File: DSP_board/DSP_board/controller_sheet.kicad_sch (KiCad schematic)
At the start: 29 parts, among them IC5 F280025CPNQR, J1 Conn_01x02, J2 Conn_01x02, J3 Conn_01x02, J4 Conn_01x02, J5 1-84981-0, J6 Conn_01x02

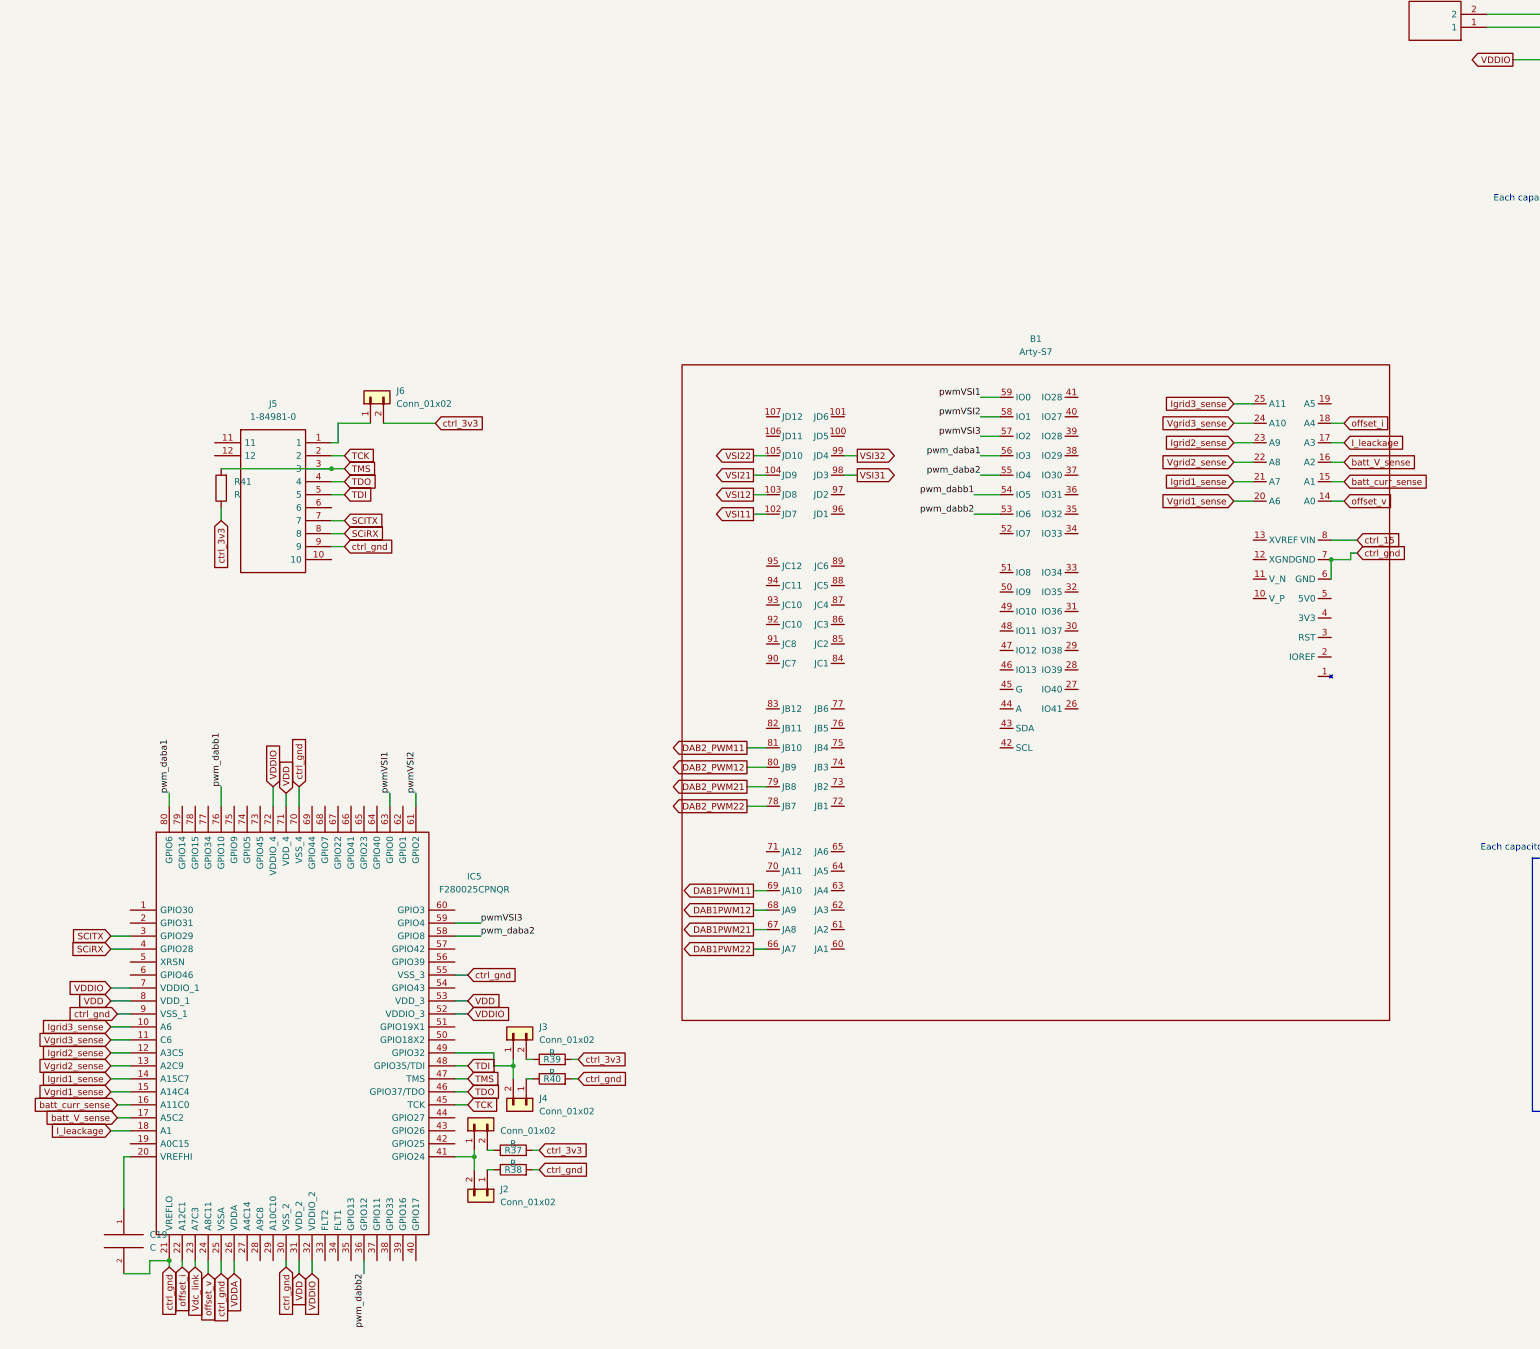
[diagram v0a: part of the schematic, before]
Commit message: adding diodes
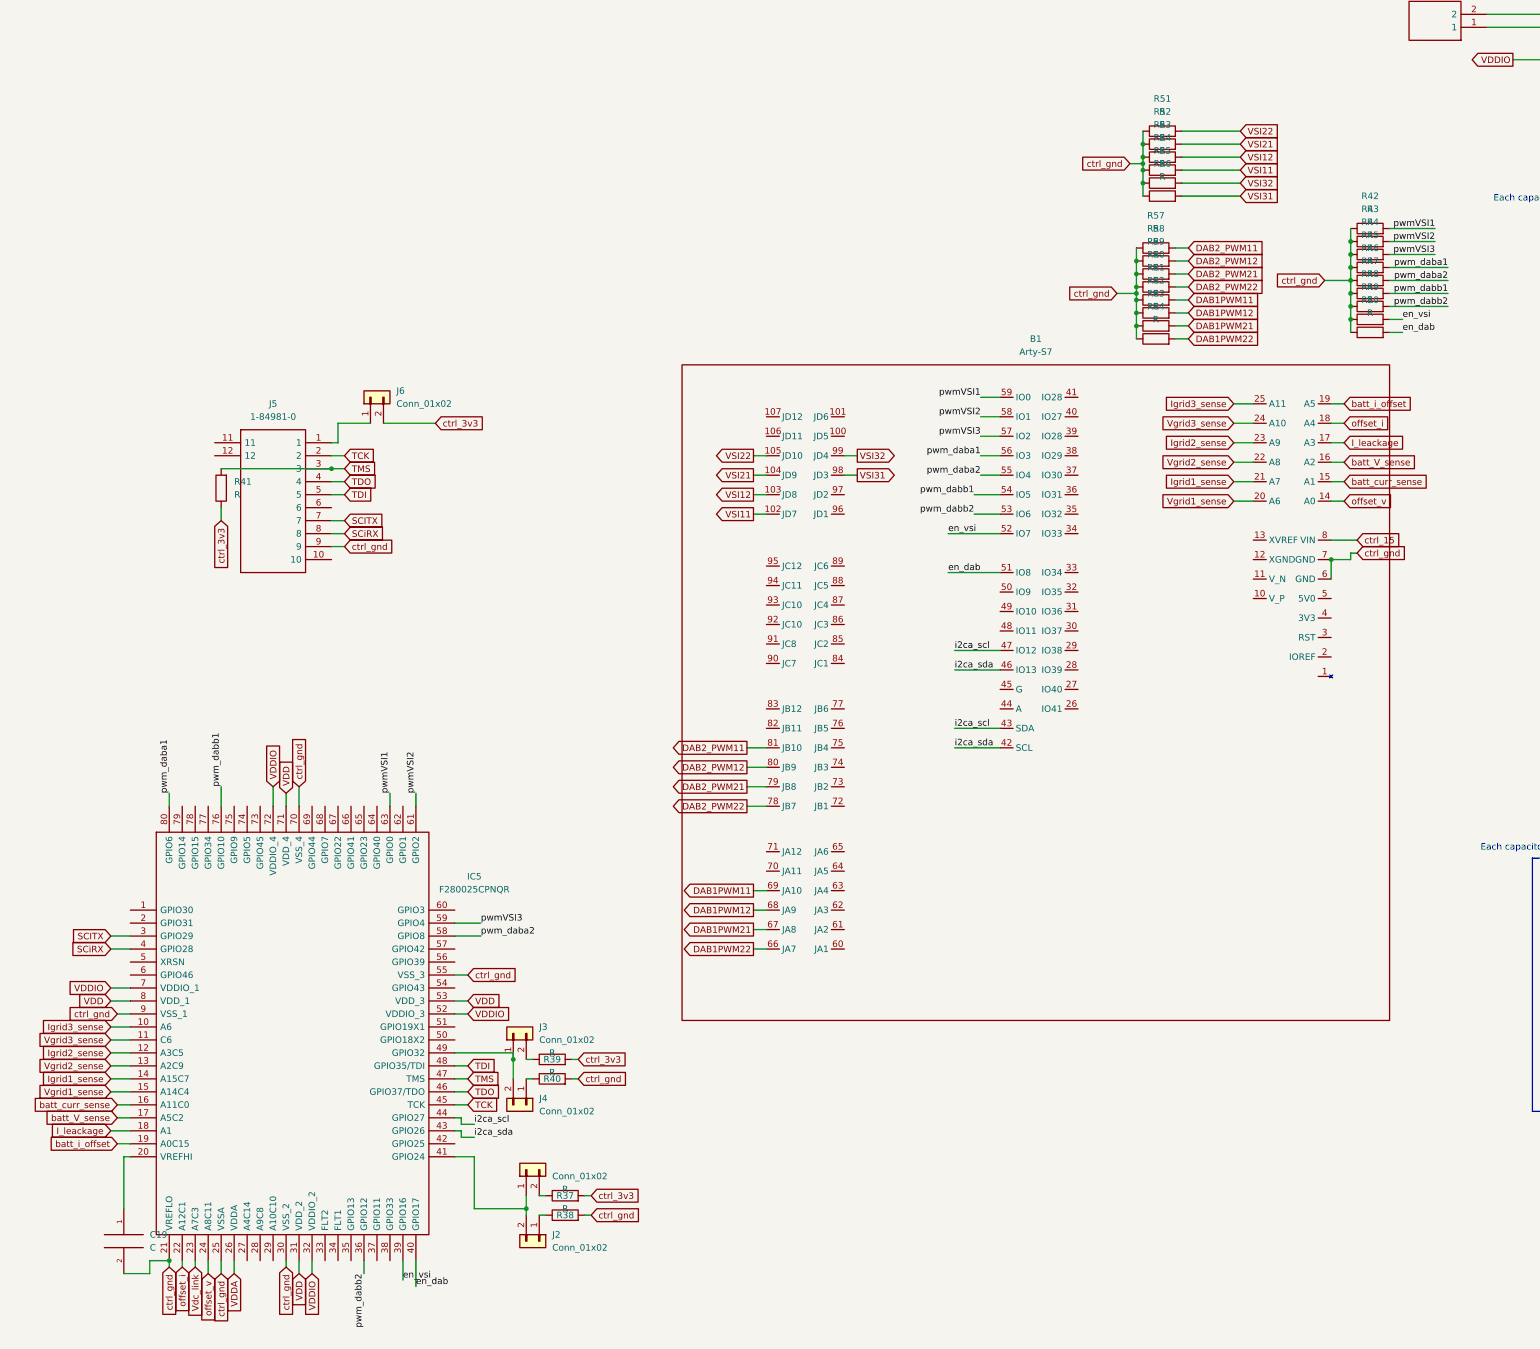
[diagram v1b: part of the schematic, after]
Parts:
- added R42, R43, R44, R45, R46, R47, R48, R49, R50, R51, R52, R53, R54, R55, R56, R57, R58, R59, R60, R61, R62, R63, R64: R, Capacitor_SMD:C_1206_3216Metric_Pad1.33x1.80mm_HandSolder, symbol Device:R
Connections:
- net DAB1PWM11: now also R61.2
- net DAB1PWM12: now also R62.2
- net DAB1PWM21: now also R63.2
- net DAB1PWM22: now also R64.2
- net DAB2_PWM11: now also R57.2
- net DAB2_PWM12: now also R58.2
- net DAB2_PWM21: now also R59.2
- net DAB2_PWM22: now also R60.2
- net VSI11: now also R54.2
- net VSI12: now also R53.2
- net VSI21: now also R52.2
- net VSI22: now also R51.2
- net VSI31: now also R56.2
- net VSI32: now also R55.2
- net ctrl_gnd: now also R42.1, R43.1, R44.1, R45.1, R46.1, R47.1, R48.1, R49.1, R50.1, R51.1, R52.1, R53.1, R54.1, R55.1, R56.1, R57.1, R58.1, R59.1, R60.1, R61.1, R62.1, R63.1, R64.1
- net pwmVSI1: now also R42.2
- net pwmVSI2: now also R43.2
- net pwmVSI3: now also R44.2
- net pwm_daba1: now also R45.2
- net pwm_daba2: now also R46.2
- net pwm_dabb1: now also R47.2
- net pwm_dabb2: now also R48.2
- net batt_i_offset: now reaches IC5.19 (A0C15)
- net batt_i_offset: now also B1.19 (A5)
- net en_vsi: now reaches IC5.39 (GPIO16)
- net en_vsi: now also B1.52 (IO7), R49.2
- net en_dab: now reaches IC5.40 (GPIO17)
- net en_dab: now also B1.51 (IO8), R50.2
- net i2ca_sda: now reaches IC5.43 (GPIO26)
- net i2ca_sda: now also B1.42 (SCL), B1.46 (IO13)
- net i2ca_scl: now reaches IC5.44 (GPIO27)
- net i2ca_scl: now also B1.43 (SDA), B1.47 (IO12)
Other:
- moved on the sheet: J2, R37, R38

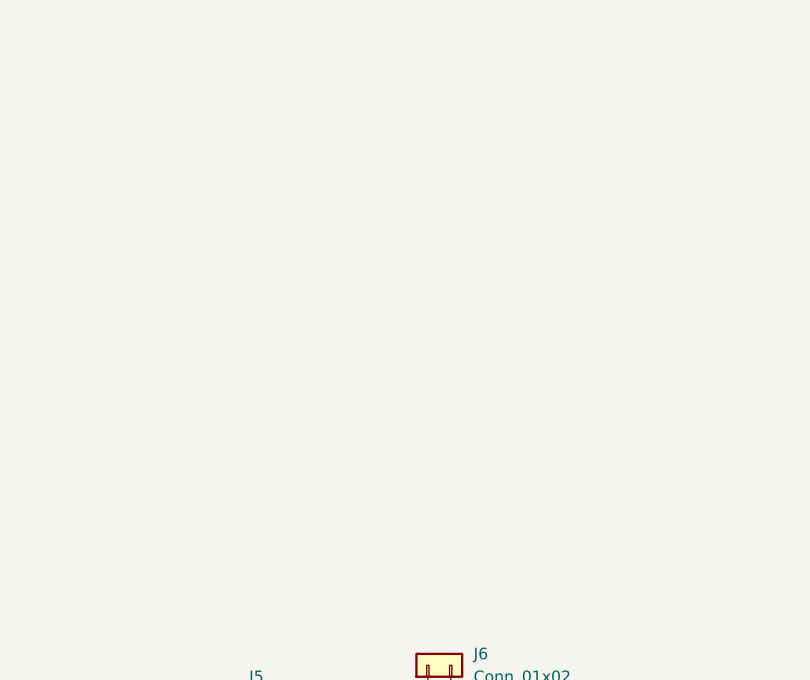
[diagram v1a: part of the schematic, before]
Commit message: adding diode footprint
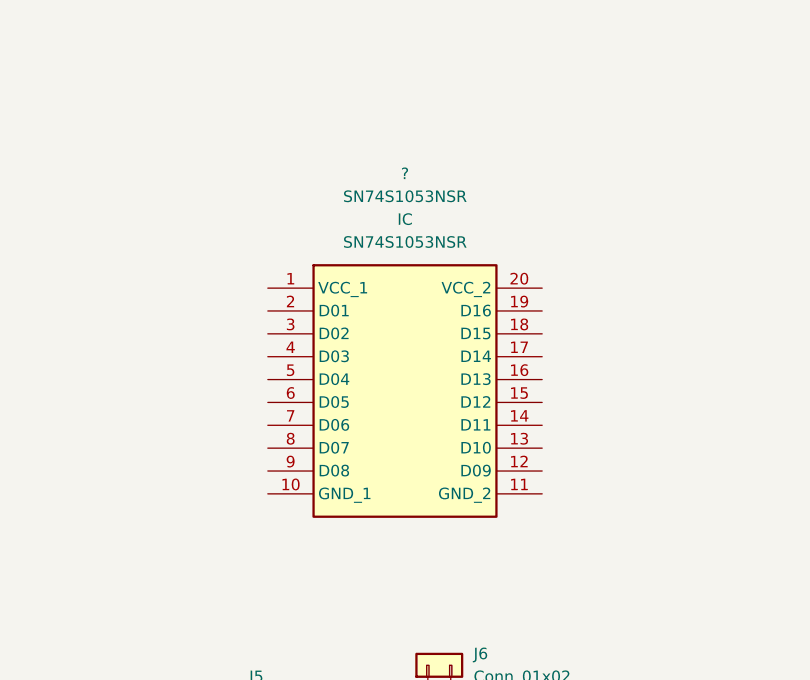
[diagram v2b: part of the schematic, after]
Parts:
- added ?: SN74S1053NSR, symbol SN74S1053NSR:SN74S1053NSR
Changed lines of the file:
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@@
     (pin "2")
+  )
+  (symbol (lib_id "SN74S1053NSR:SN74S1053NSR") (at 62.23 60.96 0) (unit 1)
+    (in_bom yes) (on_board yes) (fields_autoplaced)
+    (property "Reference" "?" (id 0) (at 77.47 48.26 0))
+    (property "Value" "SN74S1053NSR" (id 1) (at 77.47 50.8 0))
+    (property "Footprint" "" (id 2) (at 62.23 60.96 0)
+      (effects (font (size 1.27 1.27)) hide)
+    )
+    (property "Datasheet" "" (id 3) (at 62.23 60.96 0)
+      (effects (font (size 1.27 1.27)) hide)
+    )
+    (property "Reference_1" "IC" (id 4) (at 77.47 53.34 0))
+    (property "Value_1" "SN74S1053NSR" (id 5) (at 77.47 55.88 0))
+    (property "Footprint_1" "SOIC127P780X200-20N" (id 6) (at 88.9 155.88 0)
+      (effects (font (size 1.27 1.27)) (justify left top) hide)
+    )
+    (property "Datasheet_1" "http://www.ti.com/lit/gpn/sn74s1053" (id 7) (at 88.9 255.88 0)
+      (effects (font (size 1.27 1.27)) (justify left top) hide)
+    )
+    (property "Height" "2" (id 8) (at 88.9 455.88 0)
+      (effects (font (size 1.27 1.27)) (justify left top) hide)
+    )
+    (property "Mouser Part Number" "595-SN74S1053NSR" (id 9) (at 88.9 555.88 0)
+      (effects (font (size 1.27 1.27)) (justify left top) hide)
+    )
+    (property "Mouser Price/Stock" "https://www.mouser.co.uk/ProductDetail/Texas-Instruments/SN74S1053NSR?qs=gb35HGp1gQKBVeOxZl0Yrw%3D%3D" (id 10) (at 88.9 655.88 0)
+      (effects (font (size 1.27 1.27)) (justify left top) hide)
+    )
+    (property "Manufacturer_Name" "Texas Instruments" (id 11) (at 88.9 755.88 0)
+      (effects (font (size 1.27 1.27)) (justify left top) hide)
+    )
+    (property "Manufacturer_Part_Number" "SN74S1053NSR" (id 12) (at 88.9 855.88 0)
+      (effects (font (size 1.27 1.27)) (justify left top) hide)
+    )
+    (pin "1")
+    (pin "10")
+    (pin "11")
+    (pin "12")
+    (pin "13")
+    (pin "14")
+    (pin "15")
+    (pin "16")
+    (pin "17")
+    (pin "18")
+    (pin "19")
+    (pin "2")
+    (pin "20")
+    (pin "3")
+    (pin "4")
+    (pin "5")
+    (pin "6")
+    (pin "7")
+    (pin "8")
+    (pin "9")
   )
   (symbol (lib_id "Device:R") (at 275.59 74.93 90) (unit 1)
